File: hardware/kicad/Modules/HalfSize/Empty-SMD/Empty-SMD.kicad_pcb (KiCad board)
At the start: 2 copper layers, 38 x 32 mm, 4 parts, among them J1 Conn_02x07_Odd_Even, U1 24AA025E-OT

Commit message: Fix EEPROM values and DuoRelay R5 footprint
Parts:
- U1: value 24AA025E-OT -> 24AA025E64T-I/OT
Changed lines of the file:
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@@
 			)
 		)
-		(property "Value" "24AA025E-OT"
+		(property "Value" "24AA025E64T-I/OT"
 			(at 0 -2.4 0)
 			(layer "B.Fab")

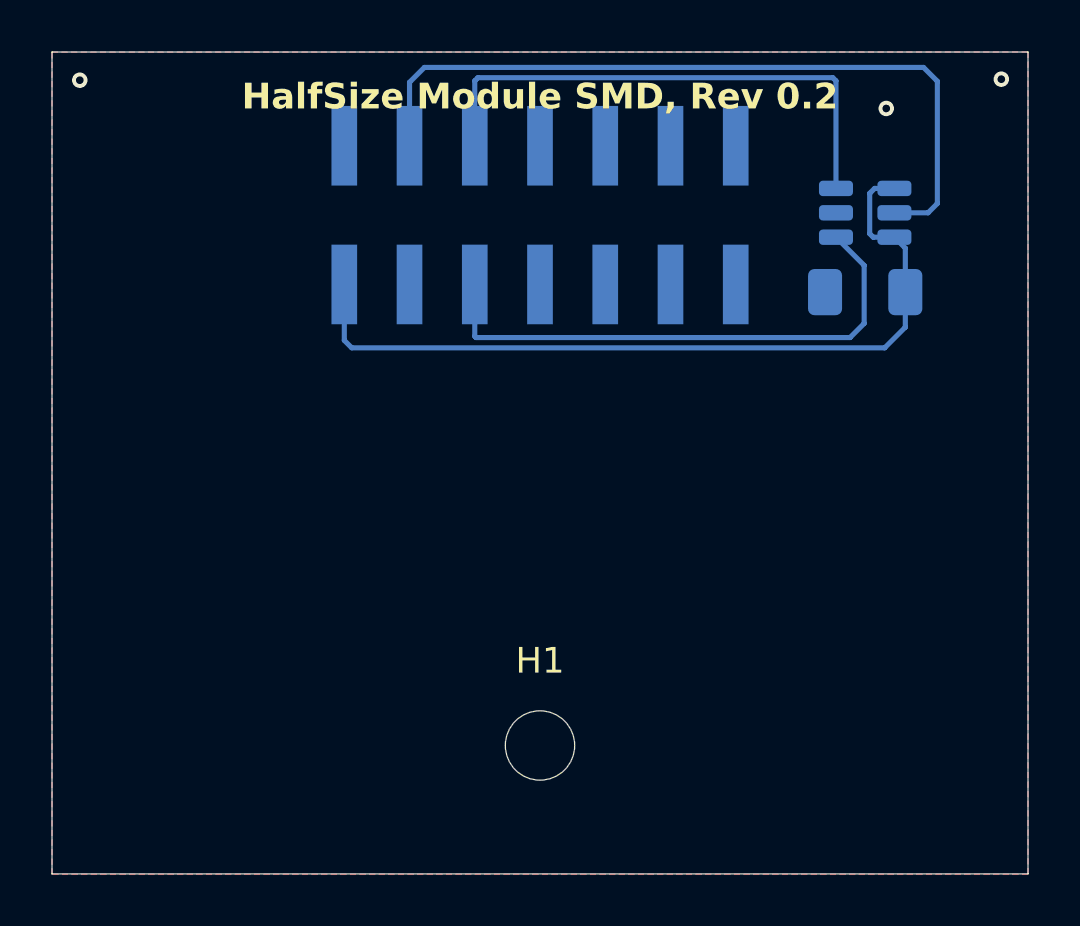
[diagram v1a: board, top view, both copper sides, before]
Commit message: Update module layouts for Rev 0.3
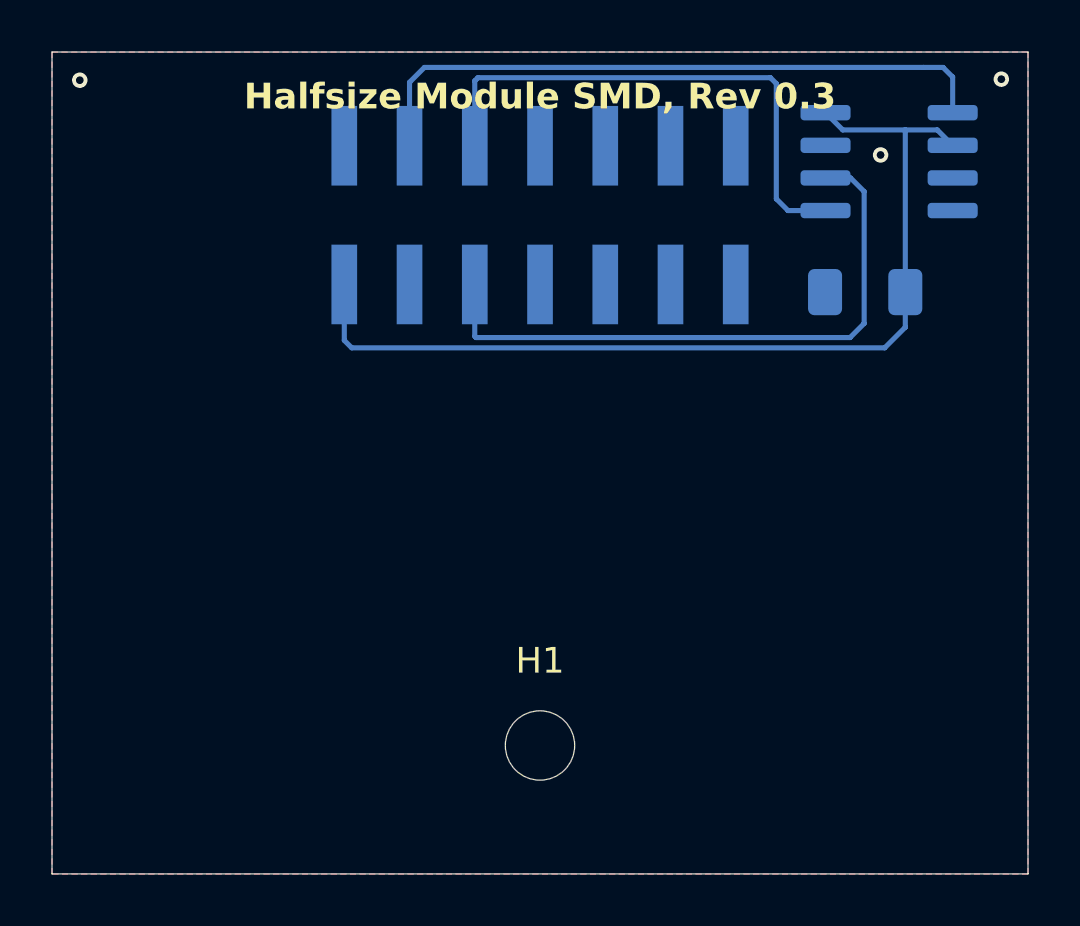
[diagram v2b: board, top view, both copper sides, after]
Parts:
- removed U1: 24AA025E64T-I/OT, Package_TO_SOT_SMD:SOT-23-6
- added U2: 24LC32, Package_SO:SOIC-8_3.9x4.9mm_P1.27mm, B.Cu at (150.4, 36.5)
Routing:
- net +3V3_SYS: track 31.8 -> 37.6 mm
- net /EEPROM_A0: track 30.1 -> 25.4 mm
- net I2C0_SCL: track 21.2 -> 24.3 mm
